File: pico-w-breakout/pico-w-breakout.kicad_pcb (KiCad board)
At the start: 2 copper layers, 44 x 59 mm, 8 parts, among them J1 Conn_01x20, J2 Conn_01x20, J3 Conn_01x20, J4 Conn_01x20, J5 Conn_01x03, J6 Conn_01x03

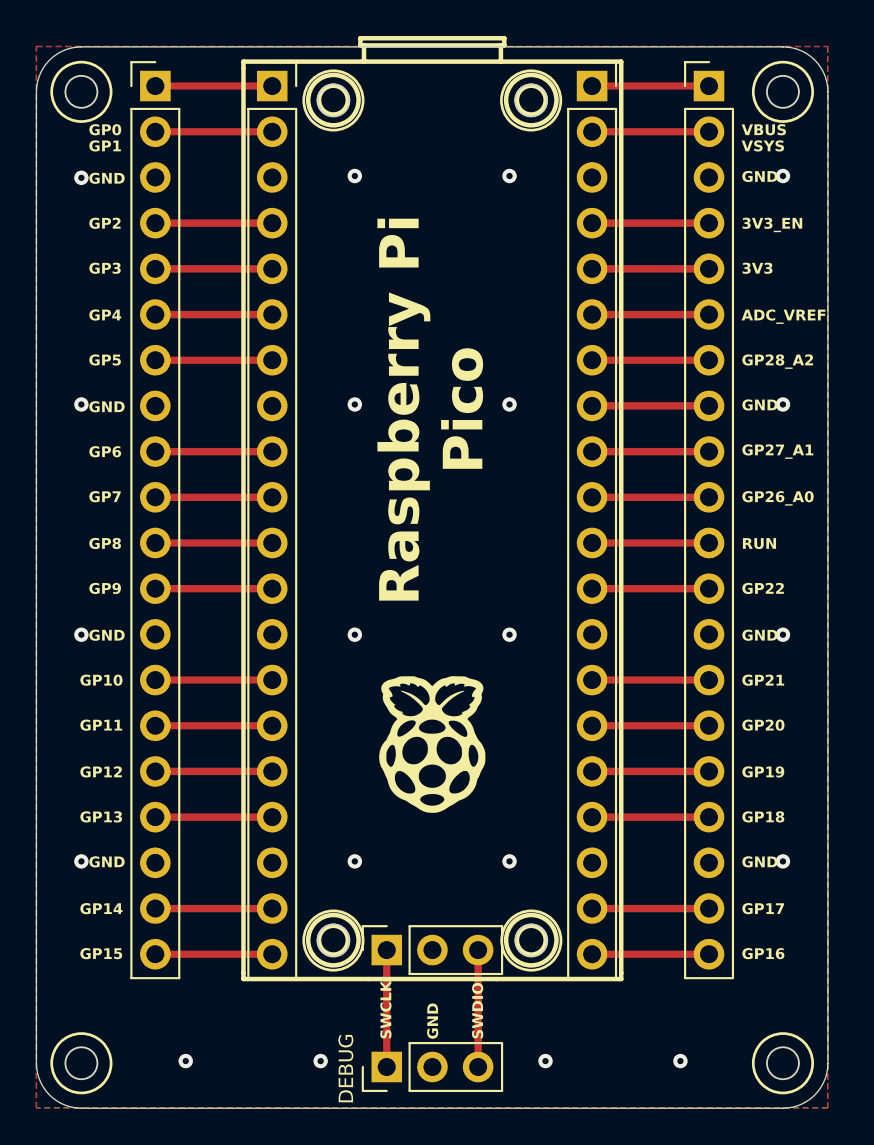
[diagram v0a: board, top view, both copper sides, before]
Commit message: Add Raspberry Pi Pico W breakout board
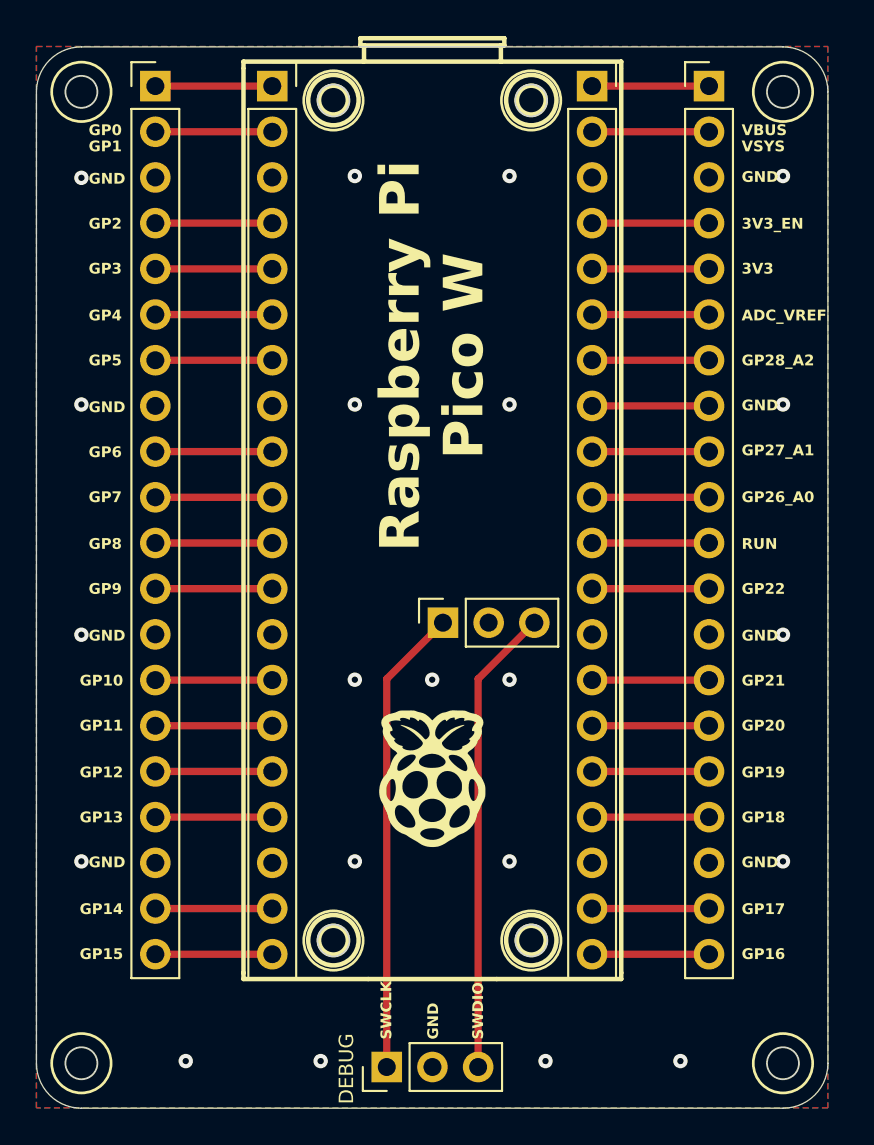
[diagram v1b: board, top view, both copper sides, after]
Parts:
- moved J6 18.5 mm to (60.4, 69.9)
- moved G*** 1.90 mm to (59.8, 78.6)
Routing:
- net Net-(J5-Pin_3): track 6.50 -> 26.0 mm
- net Net-(J5-Pin_1): track 6.50 -> 26.0 mm
- net GND: vias 20 -> 21
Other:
- board text added: "Pico W Breakout Rev.1"
- board text added: "Raspberry Pi Pico W"
- board text removed: "Pico Breakout Rev.1"
- board text removed: "Raspberry Pi Pico"
